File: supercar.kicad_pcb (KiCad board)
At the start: 2 copper layers, 63.5 x 43.6 mm, 41 parts, among them SW1 Power, U1 74HC283, U2 74HC574, U3 74HC154, U4 74HC574, U5 74HC86, U6 NE555D

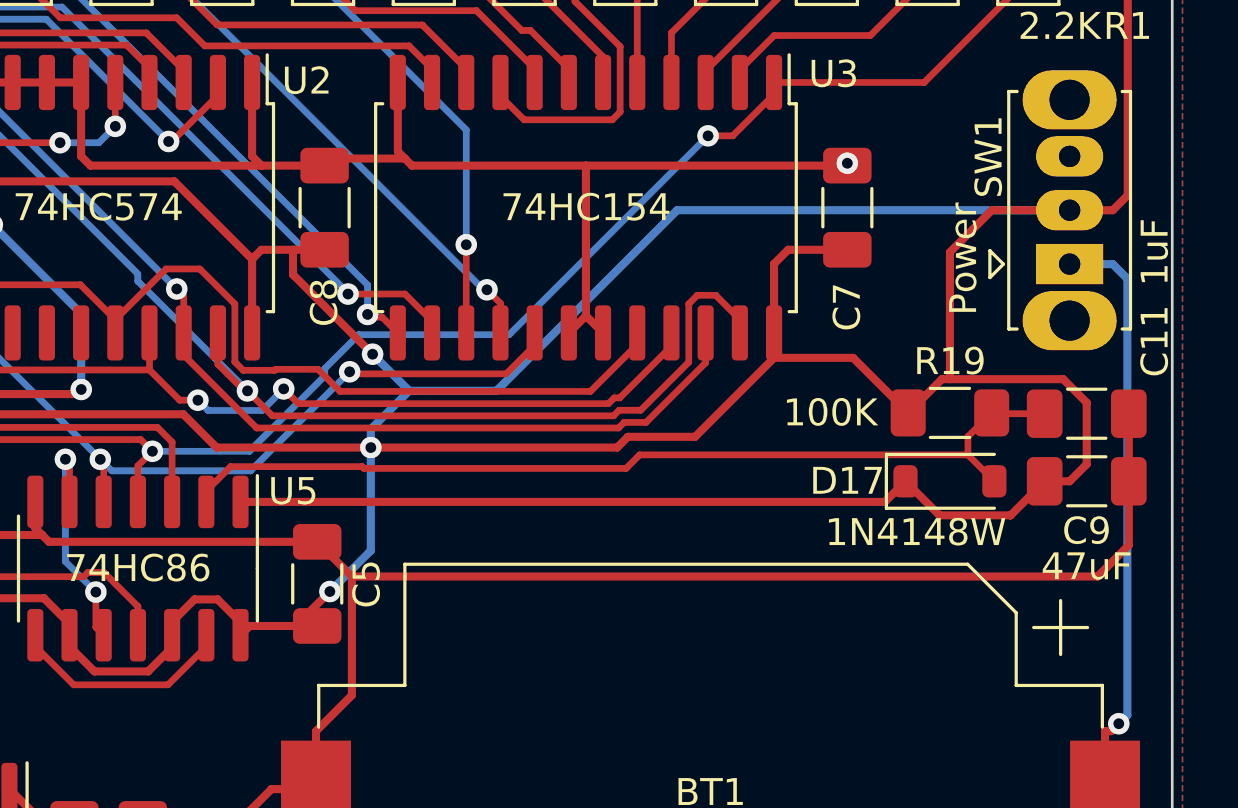
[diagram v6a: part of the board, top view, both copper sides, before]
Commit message: Change reset circuit to not turn on leds
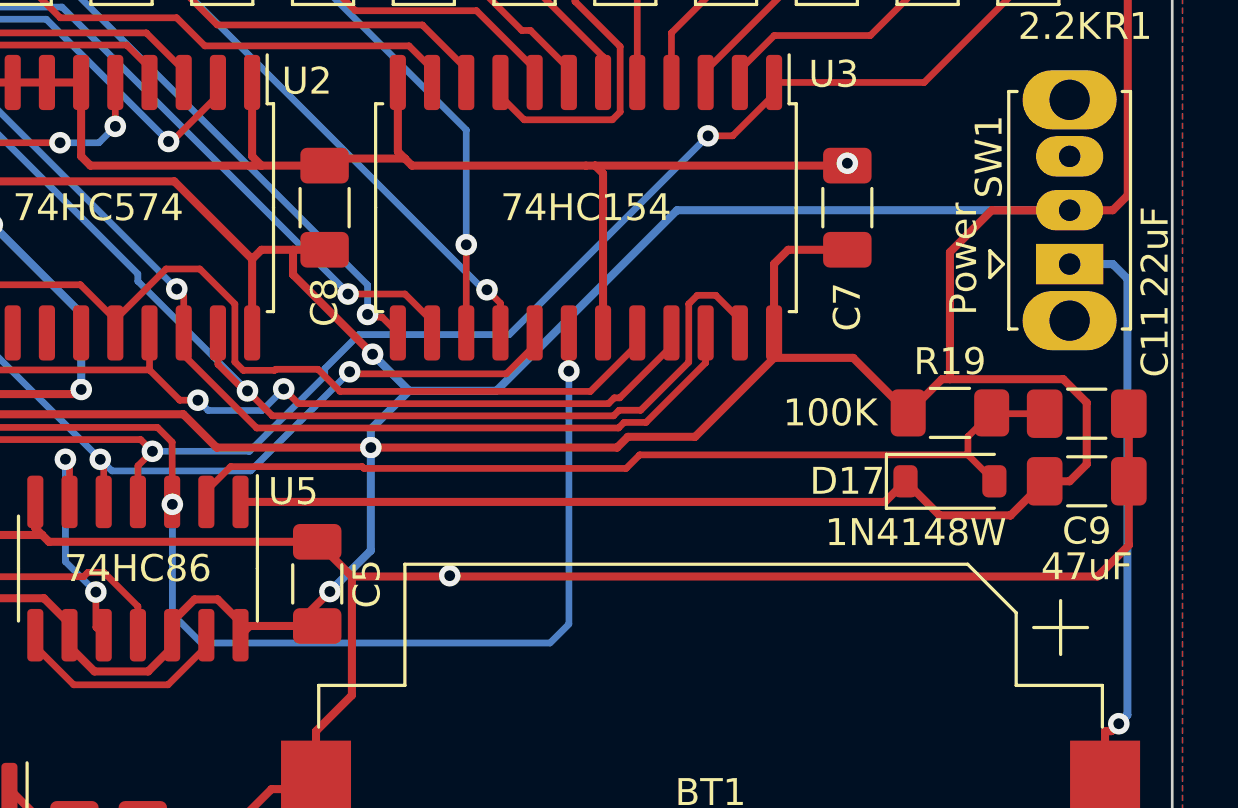
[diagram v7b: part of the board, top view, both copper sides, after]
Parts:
- C11: value 1uF -> 22uF
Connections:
- U3 pad 18: GND -> /RST
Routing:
- net /RST: track 13.8 -> 44.3 mm, vias 0 -> 2
- net GND: track 206.8 -> 205.8 mm, vias 6 -> 7
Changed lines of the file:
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@@
         (effects (font (size 1 1) (thickness 0.15)))
     )
-    (fp_text value "1uF" (at 2.54 -5.999 -90) (layer "F.SilkS")
+    (fp_text value "22uF" (at 2.54 -5.999 -90) (layer "F.SilkS")
         (effects (font (size 1 1) (thickness 0.15)))
     )
@@
       (net 6 "/LAST_BIT") (pinfunction "S15") (pintype "output"))
     (pad "18" smd roundrect (at 4.65 0.635 270) (size 2.05 0.6) (layers "F.Cu" "F.Paste" "F.Mask") (roundrect_rratio 0.25)
-      (net 2 "GND") (pinfunction "E0") (pintype "input"))
+      (net 48 "/RST") (pinfunction "E0") (pintype "input"))
     (pad "19" smd roundrect (at 4.65 -0.635 270) (size 2.05 0.6) (layers "F.Cu" "F.Paste" "F.Mask") (roundrect_rratio 0.25)
       (net 2 "GND") (pinfunction "E1") (pintype "input"))
@@
   (segment (start 86.065 66.9) (end 85.905 66.9) (width 0.3) (layer "F.Cu") (net 2))
   (segment (start 101.434 56.2225) (end 101.087 55.875) (width 0.3) (layer "F.Cu") (net 2))
+  (segment (start 120.469 56.5165) (end 120.175 56.2225) (width 0.3) (layer "F.Cu") (net 2))
   (segment (start 107.437 55.875) (end 107.437 53.135) (width 0.3) (layer "F.Cu") (net 2))
   (segment (start 91.9865 80.264) (end 91.948 80.264) (width 0.3) (layer "F.Cu") (net 2))
-  (segment (start 129.3363 56.2225) (end 119.834 56.2225) (width 0.3) (layer "F.Cu") (net 2))
   (segment (start 86.5 63.16) (end 86.065 63.16) (width 0.3) (layer "F.Cu") (net 2))
   (segment (start 83.365 66.9) (end 82.095 66.9) (width 0.3) (layer "F.Cu") (net 2))
@@
   (segment (start 84.635 66.9) (end 83.365 66.9) (width 0.3) (layer "F.Cu") (net 2))
   (segment (start 139.9925 67.945) (end 139.9925 65.435) (width 0.3) (layer "F.Cu") (net 2))
+  (segment (start 114.775 71.45) (end 114.8051 71.4801) (width 0.3) (layer "F.Cu") (net 2))
   (segment (start 85.905 66.9) (end 84.635 66.9) (width 0.3) (layer "F.Cu") (net 2))
   (segment (start 97.277 53.135) (end 96.007 53.135) (width 0.3) (layer "F.Cu") (net 2))
-  (segment (start 119.834 56.2225) (end 119.834 61.8) (width 0.3) (layer "F.Cu") (net 2))
   (segment (start 103.378 80.4795) (end 100.838 80.4795) (width 0.3) (layer "F.Cu") (net 2))
   (segment (start 93.316 54.766) (end 93.218 54.864) (width 0.3) (layer "F.Cu") (net 2))
@@
   (segment (start 99.5151 80.4651) (end 99.2547 80.7255) (width 0.3) (layer "F.Cu") (net 2))
   (segment (start 87.175 66.9) (end 86.065 66.9) (width 0.3) (layer "F.Cu") (net 2))
-  (segment (start 119.834 61.8) (end 119.199 62.435) (width 0.3) (layer "F.Cu") (net 2))
   (segment (start 99.8942 70.1925) (end 99.6404 69.9387) (width 0.3) (layer "F.Cu") (net 2))
   (segment (start 92.448 80.7255) (end 91.9865 80.264) (width 0.3) (layer "F.Cu") (net 2))
   (segment (start 110.128 56.2225) (end 107.784 56.2225) (width 0.3) (layer "F.Cu") (net 2))
-  (segment (start 111.1426 71.4801) (end 138.8319 71.4801) (width 0.3) (layer "F.Cu") (net 2))
+  (segment (start 111.1426 71.4801) (end 114.7449 71.4801) (width 0.3) (layer "F.Cu") (net 2))
   (segment (start 99.3867 69.685) (end 99.3867 68.71) (width 0.3) (layer "F.Cu") (net 2))
   (segment (start 113.1104 55.9606) (end 112.849 55.699) (width 0.3) (layer "F.Cu") (net 2))
+  (segment (start 114.7449 71.4801) (end 114.775 71.45) (width 0.3) (layer "F.Cu") (net 2))
+  (segment (start 120.469 62.435) (end 120.469 56.5165) (width 0.3) (layer "F.Cu") (net 2))
   (segment (start 139.9925 70.3195) (end 139.9925 67.945) (width 0.3) (layer "F.Cu") (net 2))
   (segment (start 99.5151 80.4651) (end 98.425 79.375) (width 0.3) (layer "F.Cu") (net 2))
@@
   (segment (start 93.218 54.864) (end 83.939 54.864) (width 0.3) (layer "F.Cu") (net 2))
   (segment (start 129.54 56.134) (end 129.3363 56.2225) (width 0.3) (layer "F.Cu") (net 2))
+  (segment (start 114.8051 71.4801) (end 138.8319 71.4801) (width 0.3) (layer "F.Cu") (net 2))
   (segment (start 95.25 53.7058) (end 95.4362 53.7058) (width 0.3) (layer "F.Cu") (net 2))
   (segment (start 83.185 54.11) (end 83.185 53.135) (width 0.3) (layer "F.Cu") (net 2))
+  (segment (start 120.175 56.2225) (end 119.834 56.2225) (width 0.3) (layer "F.Cu") (net 2))
   (segment (start 101.087 53.135) (end 99.817 53.135) (width 0.3) (layer "F.Cu") (net 2))
   (segment (start 110.3899 55.9606) (end 110.128 56.2225) (width 0.3) (layer "F.Cu") (net 2))
-  (segment (start 120.469 62.435) (end 119.834 61.8) (width 0.3) (layer "F.Cu") (net 2))
   (segment (start 100.9212 64.706) (end 101.092 64.5352) (width 0.3) (layer "F.Cu") (net 2))
   (segment (start 86.065 63.16) (end 85.63 63.16) (width 0.3) (layer "F.Cu") (net 2))
@@
   (segment (start 103.378 80.4795) (end 107.0536 80.4795) (width 0.3) (layer "F.Cu") (net 2))
   (segment (start 113.1104 55.9606) (end 110.3899 55.9606) (width 0.3) (layer "F.Cu") (net 2))
+  (segment (start 129.3363 56.2225) (end 120.175 56.2225) (width 0.3) (layer "F.Cu") (net 2))
   (segment (start 112.849 55.699) (end 112.849 53.135) (width 0.3) (layer "F.Cu") (net 2))
   (via (at 94.996 54.61) (size 0.8) (drill 0.4) (layers "F.Cu" "B.Cu") (net 2))
   (via (at 101.092 64.5352) (size 0.8) (drill 0.4) (layers "F.Cu" "B.Cu") (net 2))
+  (via (at 114.775 71.45) (size 0.8) (drill 0.4) (layers "F.Cu" "B.Cu") (net 2))
   (via (at 129.54 56.134) (size 0.8) (drill 0.4) (layers "F.Cu" "B.Cu") (net 2))
   (via (at 97.79 58.42) (size 0.8) (drill 0.4) (layers "F.Cu" "B.Cu") (net 2))
@@
   (segment (start 99.3867 73.66) (end 99.3867 74.0777) (width 0.25) (layer "F.Cu") (net 47))
   (segment (start 99.3867 74.0777) (end 100.8111 75.5021) (width 0.25) (layer "F.Cu") (net 47))
+  (segment (start 119.199 63.849) (end 119.2 63.85) (width 0.25) (layer "F.Cu") (net 48))
   (segment (start 103.9204 65.9438) (end 94.4812 65.9438) (width 0.25) (layer "F.Cu") (net 48))
   (segment (start 94.4812 65.9438) (end 93.525 66.9) (width 0.25) (layer "F.Cu") (net 48))
   (segment (start 104.4667 66.4901) (end 103.9204 65.9438) (width 0.25) (layer "F.Cu") (net 48))
-  (segment (start 104.4667 68.71) (end 104.4667 66.4901) (width 0.25) (layer "F.Cu") (net 48))
+  (segment (start 104.4667 68.71) (end 104.475 68.8) (width 0.25) (layer "F.Cu") (net 48))
+  (segment (start 104.475 68.8) (end 104.4667 66.4901) (width 0.25) (layer "F.Cu") (net 48))
+  (segment (start 119.199 62.435) (end 119.199 63.849) (width 0.25) (layer "F.Cu") (net 48))
+  (via (at 119.2 63.85) (size 0.8) (drill 0.4) (layers "F.Cu" "B.Cu") (net 48))
+  (via (at 104.475 68.8) (size 0.8) (drill 0.4) (layers "F.Cu" "B.Cu") (net 48))
+  (segment (start 119.2 63.85) (end 119.2 73.25) (width 0.25) (layer "B.Cu") (net 48))
+  (segment (start 118.5 73.95) (end 105.55 73.95) (width 0.25) (layer "B.Cu") (net 48))
+  (segment (start 105.55 73.95) (end 104.475 72.875) (width 0.25) (layer "B.Cu") (net 48))
+  (segment (start 119.2 73.25) (end 118.5 73.95) (width 0.25) (layer "B.Cu") (net 48))
+  (segment (start 104.475 72.875) (end 104.475 68.8) (width 0.25) (layer "B.Cu") (net 48))
   (segment (start 84.455 53.135) (end 84.455 52.7033) (width 0.25) (layer "F.Cu") (net 49))
   (segment (start 81.2875 52.1097) (end 81.2875 54.7797) (width 0.25) (layer "F.Cu") (net 49))

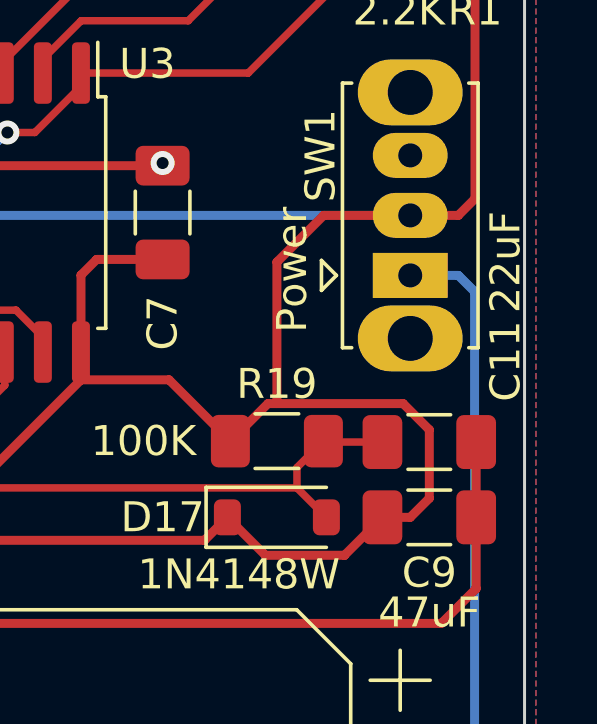
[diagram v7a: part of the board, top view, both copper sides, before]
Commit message: Small change in component value
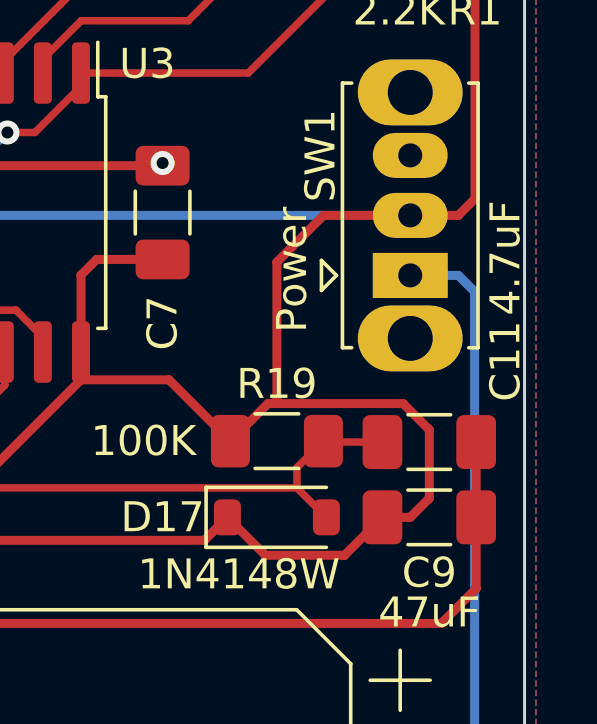
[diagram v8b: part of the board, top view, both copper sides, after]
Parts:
- C11: value 22uF -> 4.7uF
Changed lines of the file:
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@@
     (fp_line (start 1.6 0.8) (end -1.6 0.8)
       (stroke (width 0.1) (type solid)) (layer "F.Fab"))
-    (pad "1" smd roundrect (at -1.5625 0 180) (size 1.325 1.8) (layers "F.Cu" "F.Paste" "F.Mask") (roundrect_rratio 0.188679)
+    (pad "1" smd roundrect (at -1.5625 0 180) (size 1.325 1.8) (layers "F.Cu" "F.Paste" "F.Mask") (roundrect_rratio 0.1886792453)
       (net 2 "GND") (pintype "passive"))
-    (pad "2" smd roundrect (at 1.5625 0 180) (size 1.325 1.8) (layers "F.Cu" "F.Paste" "F.Mask") (roundrect_rratio 0.188679)
+    (pad "2" smd roundrect (at 1.5625 0 180) (size 1.325 1.8) (layers "F.Cu" "F.Paste" "F.Mask") (roundrect_rratio 0.1886792453)
       (net 5 "+3V3") (pintype "passive"))
     (model "${KICAD6_3DMODEL_DIR}/Capacitor_SMD.3dshapes/C_1206_3216Metric.wrl"
@@
         (effects (font (size 1 1) (thickness 0.15)))
     )
-    (fp_text value "22uF" (at 2.54 -5.999 -90) (layer "F.SilkS")
-        (effects (font (size 1 1) (thickness 0.15)))
-    )
+    (fp_text value "4.7uF" (at 2.54 -6.135 -90) (layer "F.SilkS")
+        (effects (font (size 1 1) (thickness 0.15)))
+    )
